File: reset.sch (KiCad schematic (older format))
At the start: 20 parts, among them SW2 Reset Switch, SW3 Disk Reset, U16 74LS14, U27 LM556, U30 7406, U63 7406

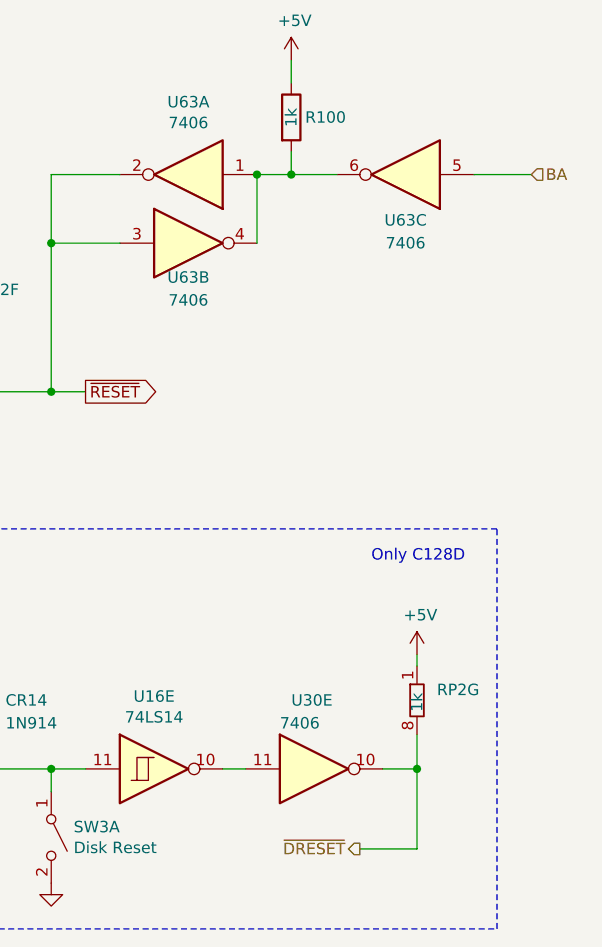
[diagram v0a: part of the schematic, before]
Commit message: Clean up schematic
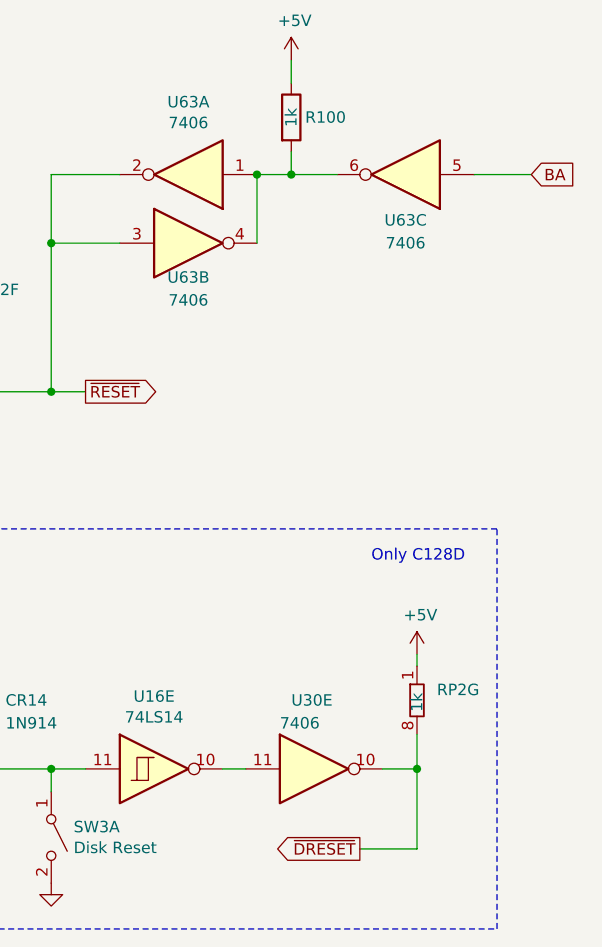
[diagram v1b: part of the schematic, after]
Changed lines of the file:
@@
 Wire Wire Line
 	7500 1850 7500 1550
-Text HLabel 9600 1550 2    50   Input ~ 0
-BA
 Wire Wire Line
 	9600 1550 9350 1550
@@
 Wire Wire Line
 	9100 4150 8950 4150
-Text HLabel 8850 4500 0    50   Output ~ 0
-~DRESET
 Wire Wire Line
 	9100 4150 9100 4500
@@
 Wire Wire Line
 	7500 4150 7650 4150
+Text GLabel 9600 1550 2    50   Input ~ 0
+BA
+Text GLabel 8850 4500 0    50   Output ~ 0
+~DRESET
 $EndSCHEMATC
